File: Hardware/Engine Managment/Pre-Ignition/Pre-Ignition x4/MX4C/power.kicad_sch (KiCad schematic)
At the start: 11 parts, among them IC1 L78M05ABDT-TR

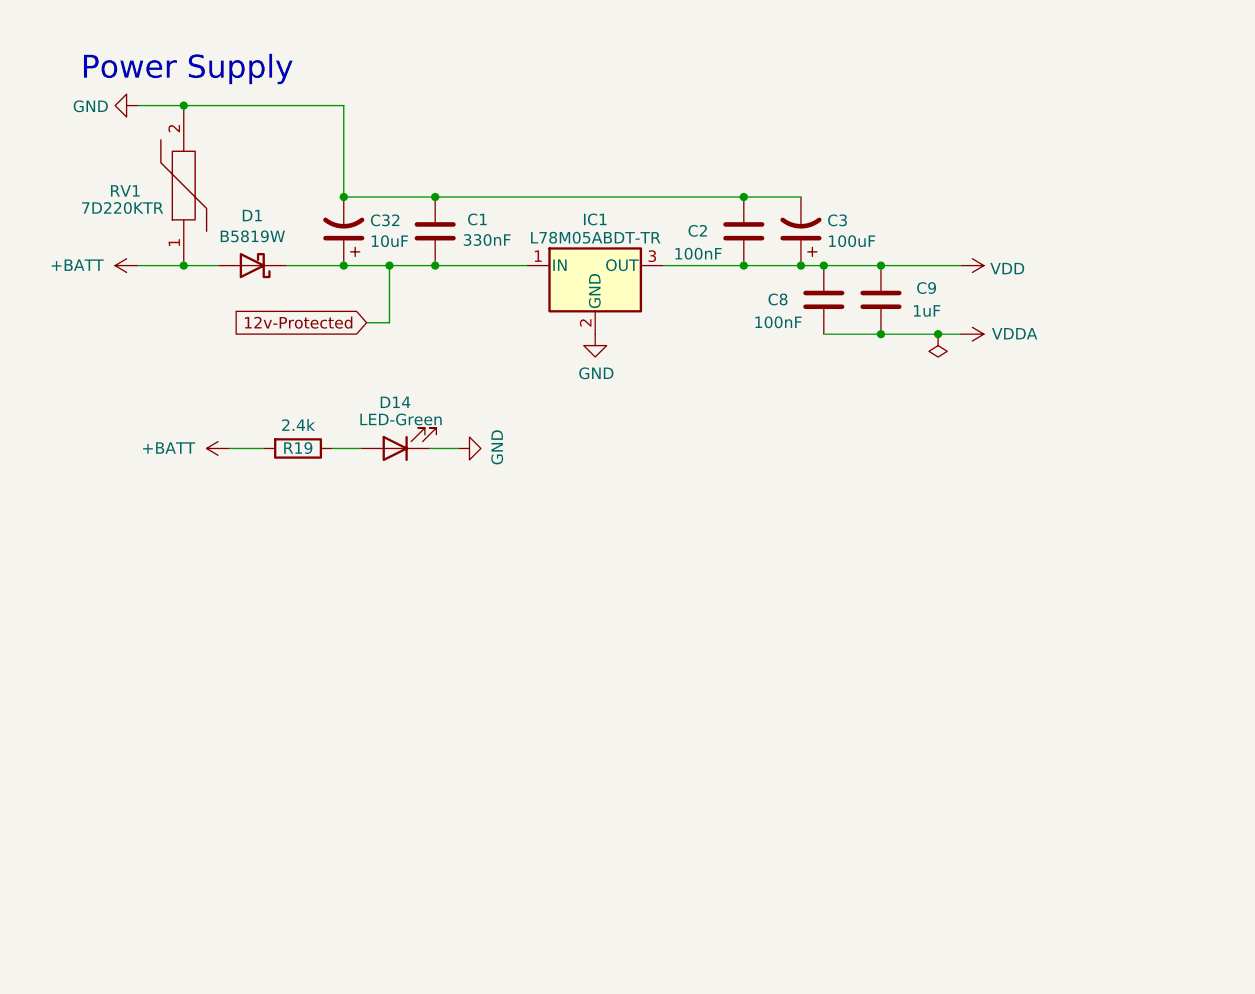
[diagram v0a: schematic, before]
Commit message: Upload correct initial upload files
Initial upload files were accidently taken from an alpha folder. 5v pins on main connector had no voltage. To fix the issue on any manufactured boards remove C8 and C9. Then short the pins of the removed capacitors.
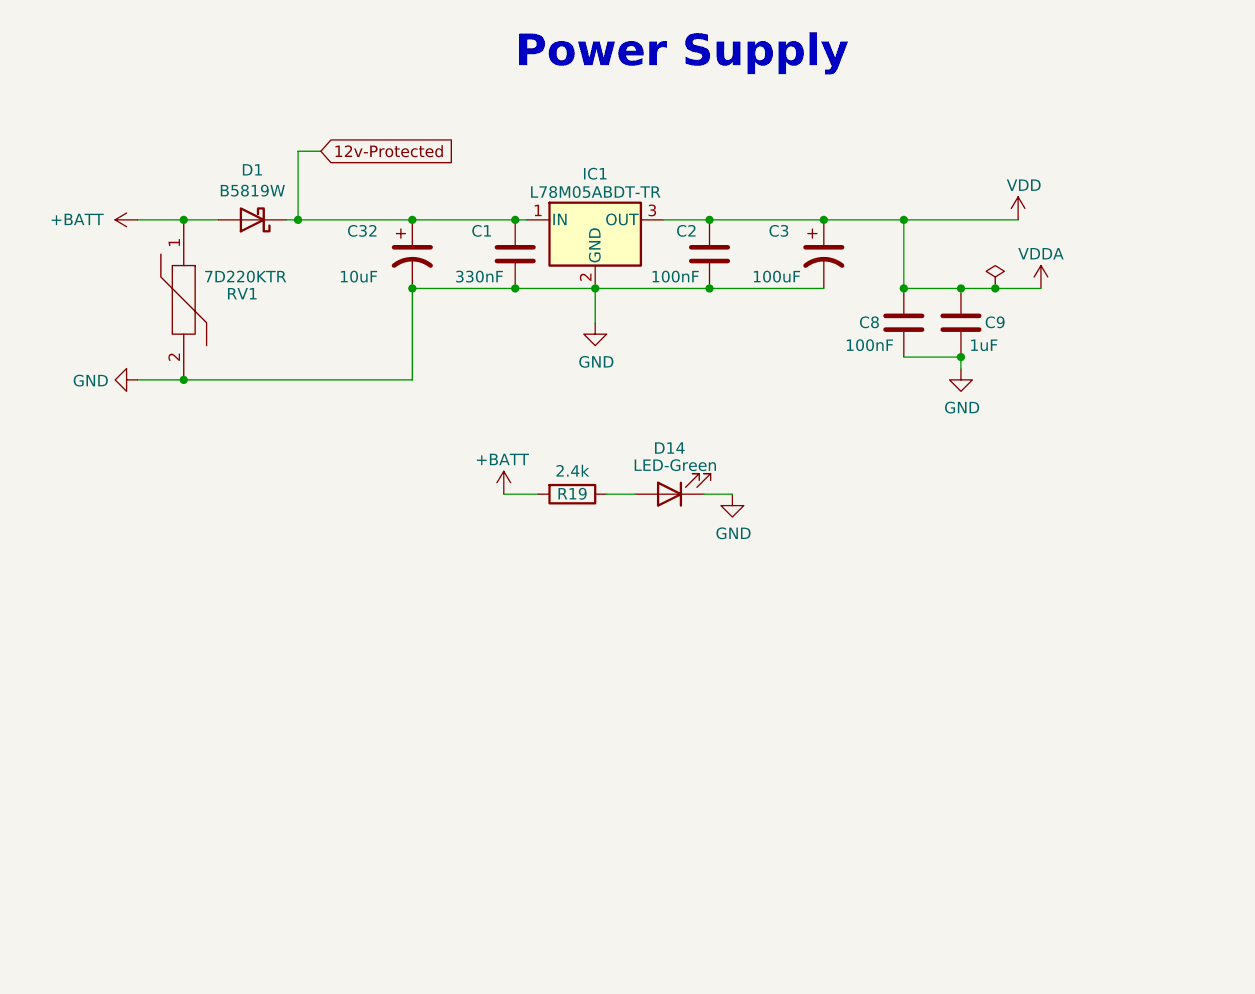
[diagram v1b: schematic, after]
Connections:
- net VDDA is gone; now on net GND: C8.2, C9.2
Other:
- company: (none) -> DetonationEMS
- title: (none) -> Pre-Ignition X4
- moved on the sheet: C1, C2, C3, C32, C8, C9, D1, D14, IC1, R19, RV1

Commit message: Structure Update
MX2 - RevB Upload
MX4B-2 - KiCad Version update (no changes)
MX4C - Organized Schematic, Minor layout change
Engine Simulator 8 Channel - Organized Schematic (no changes)
PMAP-M - Map Sensor Breakout for MX4C
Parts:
- removed C3: 100uF, Capacitor_Tantalum_SMD:CP_EIA-3528-15_AVX-H, symbol Device:CP1
- removed C32: 10uF, Capacitor_THT:CP_Radial_Tantal_D5.0mm_P2.50mm, symbol Device:C_Polarized_US
- removed C8: 100nF, Capacitor_SMD:C_0603_1608Metric, symbol Device:C
- removed C9: 1uF, Capacitor_SMD:C_0603_1608Metric, symbol Device:C
- removed IC1: L78M05ABDT-TR, Detonation:TO-252-2-Thermal-Pad, symbol Regulator_Linear:L7805
- added C3: 10uF, Capacitor_Tantalum_SMD:CP_EIA-3216-18_Kemet-A, symbol Device:C_Polarized_US
- added C30: 2.2uF, Capacitor_SMD:C_1206_3216Metric, symbol Device:C
- added D5: ZMM5V6-M, Diode_SMD:D_MiniMELF, symbol Diode:ZMMxx
- added IC3: L78M05ABDT-TR, Detonation:TO-252-2-Thermal, symbol Regulator_Linear:L7805
- D1: value B5819W -> SS34; footprint Diode_SMD:D_SOD-123 -> Diode_SMD:D_SMA; LCSC C8598 -> C8678; Manufacture Part Number B5819W -> SS34
- renumbered C2 to C3, D14 to D15
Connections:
- net GND: now also C3.2, C30.2, D5.2 (A), IC3.2 (GND)
- net 12v-Protected renamed +Batt-Protected
- net +Batt-Protected: now also C30.1, IC3.1 (IN)
- net VDD renamed +5V
- net +5V: now also C3.1, D5.1 (K), IC3.3 (OUT)
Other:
- note added: "Primary Power input"
- note added: "Research Findings: (C2 2.2uF X7R Ceramic) Automotive applications where focusing on filtering high-frequency noise and voltage spikes is important. Additional filtering on the per-regulated input using ceramic capacitors with a low ESR (X7R) provide better high-frequency noise filtering compared to tantalum capacitors."
- note added: "Research Findings: (D2 5.6v) Previously used 5.1v zener is below max output spec. Removal made output capacitors common failure points due to accidental over voltage."
- note added: "TVS 20v"
- moved on the sheet: C1, C3, D1, D15, R19, RV1

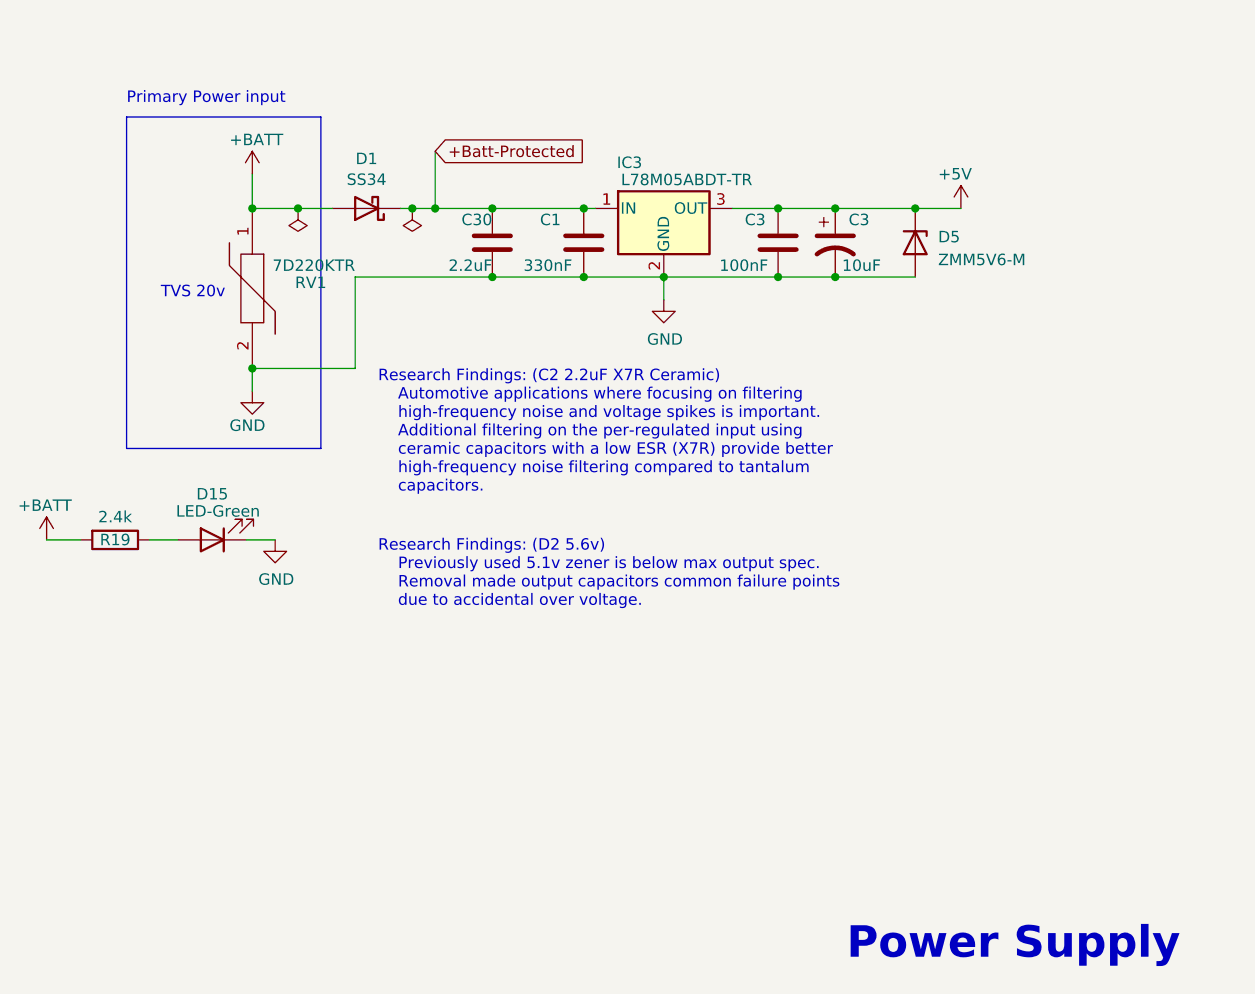
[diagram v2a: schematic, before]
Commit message: minor update
Copper Pour and clearances updated.
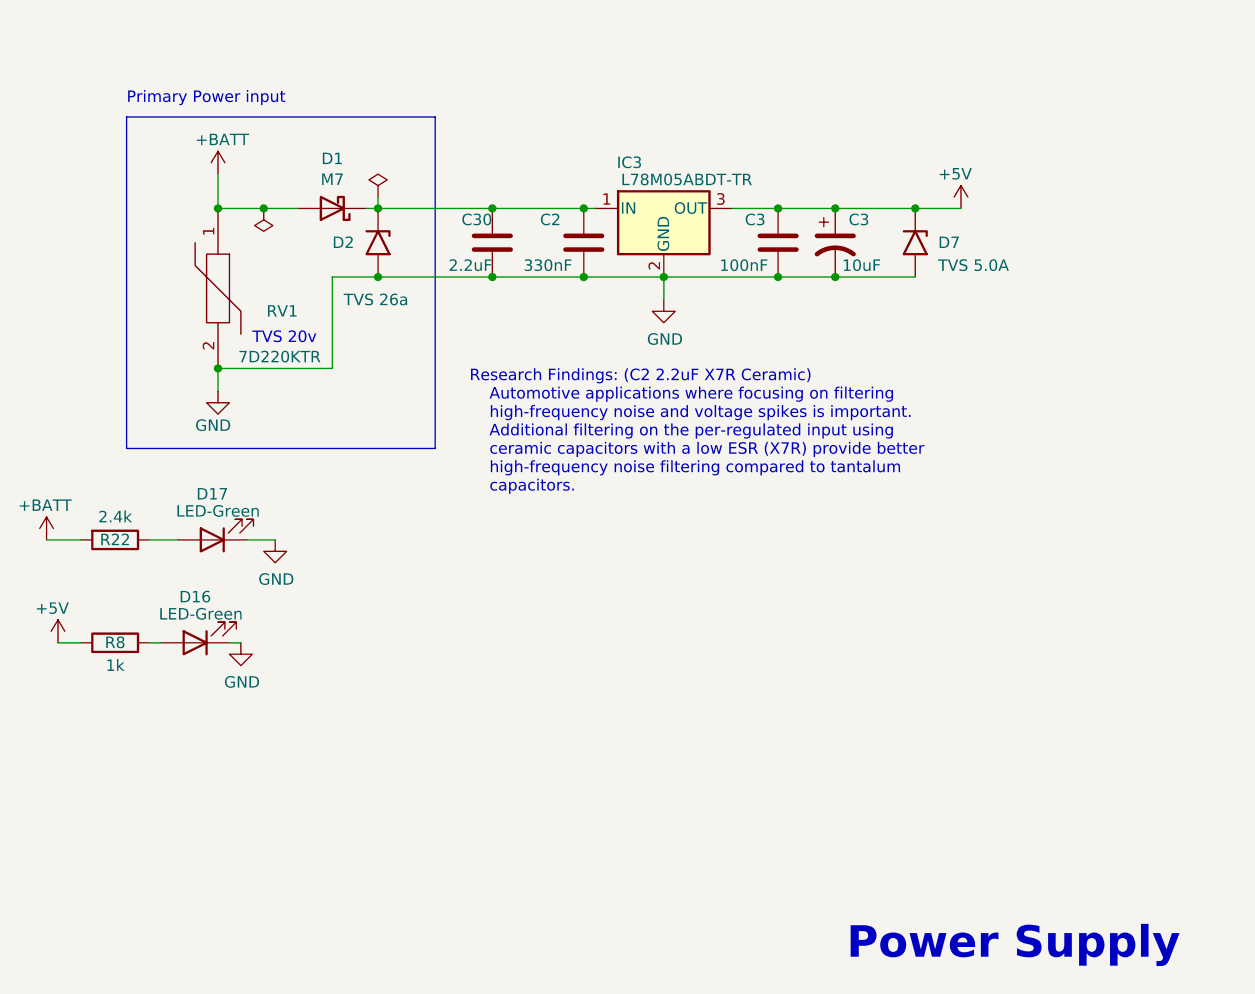
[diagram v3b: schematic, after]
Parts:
- removed D5: ZMM5V6-M, Diode_SMD:D_MiniMELF, symbol Diode:ZMMxx
- added D16: LED-Green, LED_SMD:LED_0603_1608Metric, symbol Device:LED
- added D2: TVS 26a, Diode_SMD:D_SMA, symbol Diode:SMAJ26A
- added D7: TVS 5.0A, Diode_SMD:D_SMA, symbol Diode:SMAJ5.0A
- added R8: 1k, Resistor_SMD:R_0603_1608Metric, symbol Device:R
- D1: value SS34 -> M7; LCSC C8678 -> C95872; Manufacture Part Number SS34 -> M7
- renumbered C1 to C2, D15 to D17, R19 to R22
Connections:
- net +5V: now also D7.1 (A1), R8.1
- net GND: now also D16.1 (K), D2.2 (A2), D7.2 (A2)
- net +Batt-Protected: no longer names the net of C2.1, C30.1, D1.1 (K), IC3.1 (IN)
- net +Batt-Protected: now also D2.1 (A1)
- new net: D16.2 (A), R8.2
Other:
- note removed: "Research Findings: (D2 5.6v) Previously used 5.1v zener is below max output spec. Removal made output capacitors common failure points due to accidental over voltage."
- moved on the sheet: RV1

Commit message: schematic exports
kicad version updates, schematic exports
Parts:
- renumbered C30 to C1, C3 to C4, D7 to D3, IC3 to IC1, R8 to R21
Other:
- note removed: "Research Findings: (C2 2.2uF X7R Ceramic) Automotive applications where focusing on filtering high-frequency noise and voltage spikes is important. Additional filtering on the per-regulated input using ceramic capacitors with a low ESR (X7R) provide better high-frequency noise filtering compared to tantalum capacitors."
